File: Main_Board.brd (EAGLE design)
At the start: 160.3 x 95.4 mm, 222 parts, among them J1 SERVO, J2 5.5x2.1mm Barrel, J4 BATTERY, J5 SPEAKER, J6 SDIO-SDCARD, P1 MOTOR_HEADER, P2 MOTOR_HEADER, P3 JTAG, Q1 SI9933CDY-PFET, Q2 CSD17308Q3, Q3 CSD17308Q3, Q4 CSD17308Q3, Q5 CSD17308Q3, Q6 CSD17308Q3, Q7 CSD17308Q3, Q8 CSD17308Q3, U1 LMS8117, U10 IMU, U11 LTC3122-MSOP, U12 CBAT54S-SOT23-3, U13 BQ2947, U14 TPA2005D1DGN, U15 BQ40Z60, U2 5V_BUCK_REG, U3 BTM7752G, U4 BTM7752G, U5 SN74LV4T125, U6 SN74LV4T125, U7 STM32F405RGT6, U8 RN4020RN4020, U9 BQ51013B-20VQFN, Y1 32.768KHz, Y2 25MHz

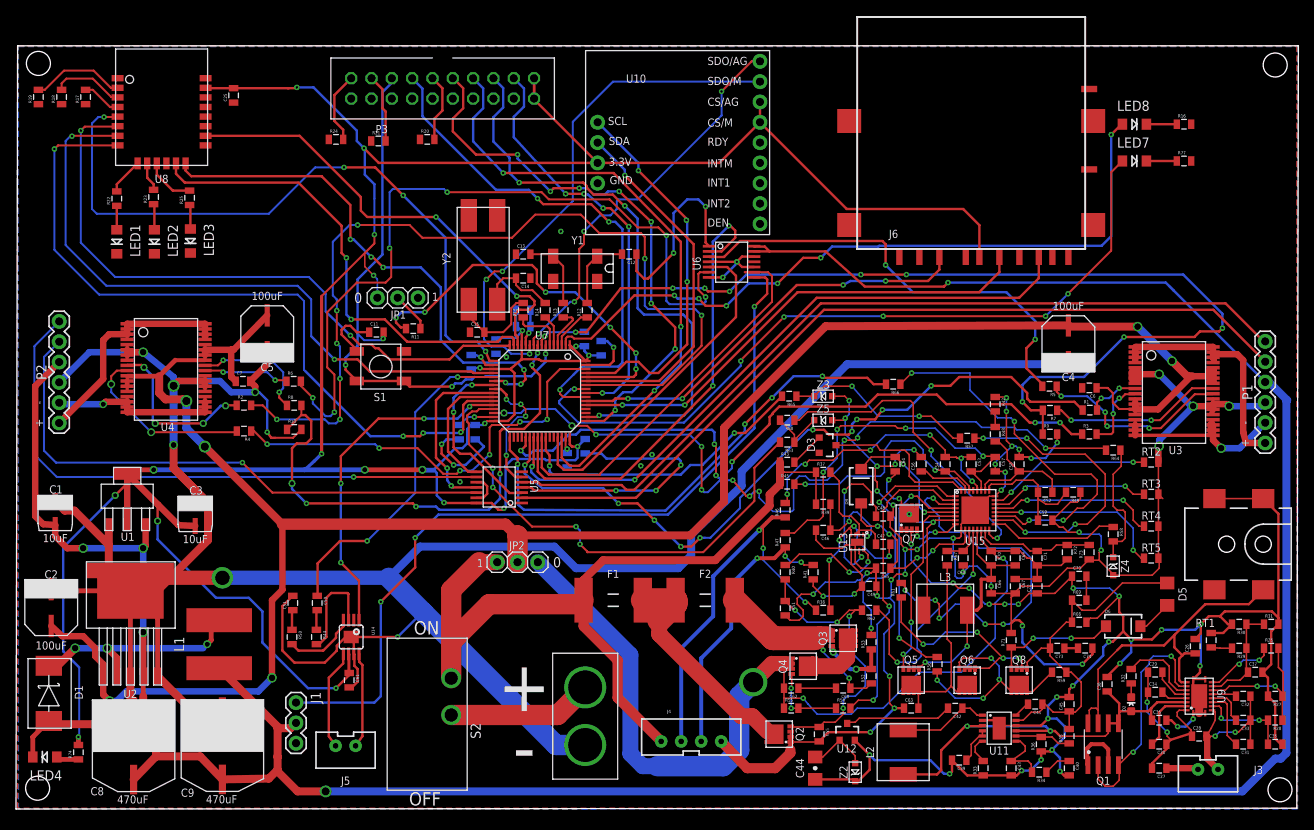
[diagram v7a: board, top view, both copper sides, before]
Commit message: added vias connecting top and bottom planes (also CAM output)
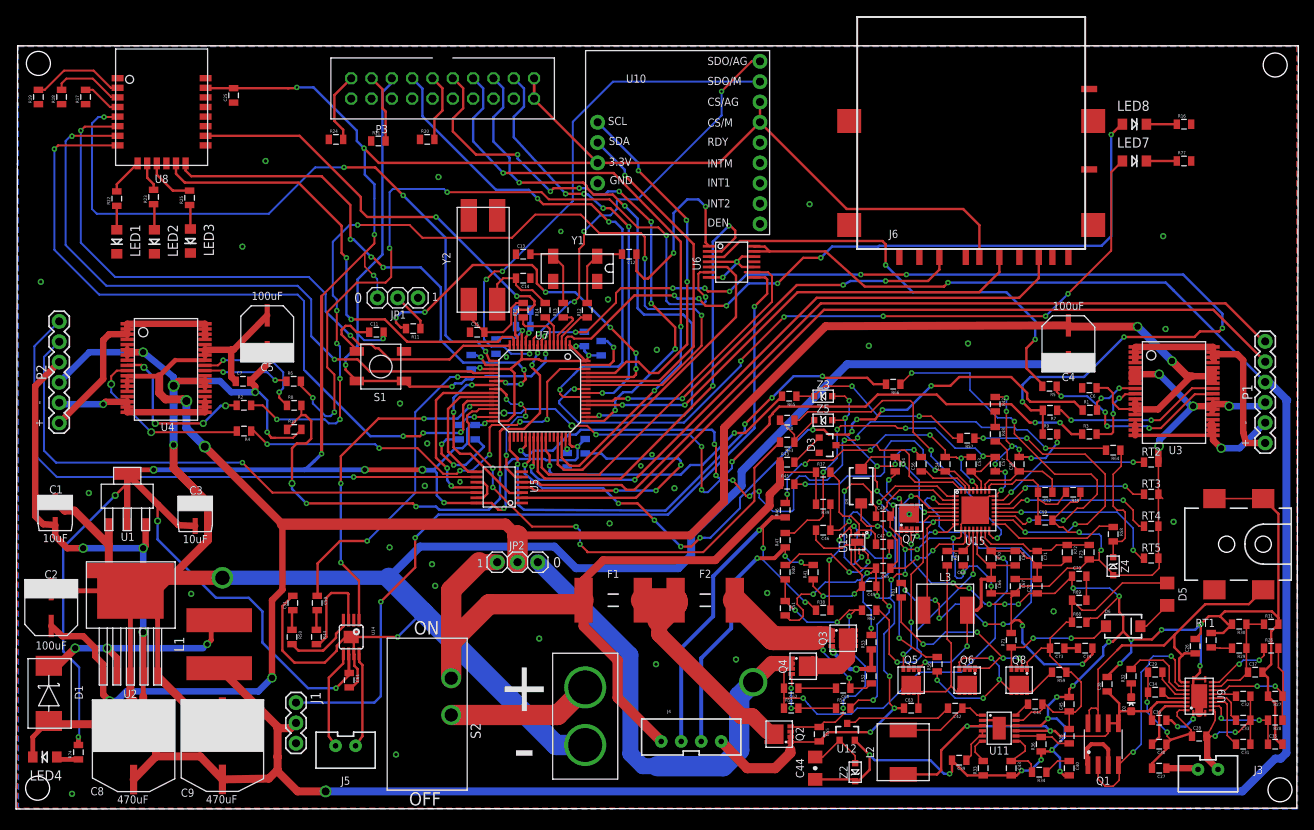
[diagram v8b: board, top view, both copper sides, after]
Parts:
- JP2: value SPDT_JUMPER -> IGNORE_CC
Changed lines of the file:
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@@
 <element name="FRAME2" library="SparkFun-Aesthetics" package="CREATIVE_COMMONS" value="FRAME-LEDGER" x="0" y="-20"/>
 <element name="FRAME3" library="SparkFun-Aesthetics" package="CREATIVE_COMMONS" value="FRAME-LEDGER" x="0" y="-20"/>
-<element name="JP2" library="BB8" package="1X03" value="SPDT_JUMPER" x="60.15" y="30.85"/>
+<element name="JP2" library="BB8" package="1X03" value="IGNORE_CC" x="60.15" y="30.85"/>
 <element name="FRAME4" library="SparkFun-Aesthetics" package="CREATIVE_COMMONS" value="FRAME-LEDGER" x="0" y="-20"/>
 <element name="FRAME5" library="SparkFun-Aesthetics" package="CREATIVE_COMMONS" value="FRAME-LEDGER" x="0" y="-20"/>
@@
 <wire x1="71.3" y1="59.6" x2="69.95" y2="59.6" width="0.3" layer="1"/>
 <via x="69.95" y="59.6" extent="1-16" drill="0.3"/>
-<wire x1="75.6" y1="65.1" x2="71.3" y2="59.6" width="0.3" layer="1"/>
 <wire x1="65.72" y1="58" x2="65.7" y2="58.02" width="0.254" layer="1"/>
 <wire x1="65.7" y1="58.02" x2="65.7" y2="58.6" width="0.254" layer="1"/>
@@
 <wire x1="66.1" y1="59.1" x2="66.6" y2="59.6" width="0.254" layer="16"/>
 <wire x1="66.6" y1="59.6" x2="69.95" y2="59.6" width="0.254" layer="16"/>
+<wire x1="71.3" y1="59.6" x2="75" y2="63.3" width="0.254" layer="1"/>
+<wire x1="75" y1="63.3" x2="75" y2="64.5" width="0.254" layer="1"/>
+<wire x1="75.6" y1="65.1" x2="75" y2="64.5" width="0.254" layer="1"/>
 </signal>
 <signal name="N$5">
@@
 <wire x1="92.9" y1="39.7" x2="92.9" y2="38.9" width="0.2" layer="16"/>
 <wire x1="59.72" y1="49.5" x2="61" y2="49.5" width="0.254" layer="1"/>
-<via x="61" y="49.5" extent="1-16" drill="0.5" shape="octagon"/>
+<via x="61" y="49.5" extent="1-16" drill="0.5"/>
 <wire x1="61" y1="49.5" x2="63.1" y2="49.5" width="0.254" layer="16"/>
 <wire x1="63.1" y1="49.5" x2="63.6" y2="50" width="0.254" layer="16"/>
@@
 <via x="68.1" y="72.2" extent="1-16" drill="0.3"/>
 </signal>
+<signal name="N$27">
+<via x="3.1" y="65.9" extent="1-16" drill="0.4"/>
+</signal>
+<signal name="N$43">
+<via x="28.3" y="70.3" extent="1-16" drill="0.4"/>
+</signal>
+<signal name="N$44">
+<via x="31.2" y="81" extent="1-16" drill="0.4"/>
+</signal>
+<signal name="N$45">
+<via x="99.2" y="75.6" extent="1-16" drill="0.4"/>
+</signal>
+<signal name="N$47">
+<via x="143.4" y="71.6" extent="1-16" drill="0.4"/>
+</signal>
+<signal name="N$130">
+<via x="106.6" y="57.9" extent="1-16" drill="0.4"/>
+</signal>
+<signal name="N$131">
+<via x="82.3" y="40.1" extent="1-16" drill="0.4"/>
+</signal>
+<signal name="N$132">
+<via x="74.2" y="35.7" extent="1-16" drill="0.4"/>
+</signal>
+<signal name="N$135">
+<via x="51.4" y="45.7" extent="1-16" drill="0.4"/>
+</signal>
+<signal name="N$136">
+<via x="51.1" y="40.4" extent="1-16" drill="0.4"/>
+</signal>
+<signal name="N$137">
+<via x="46.7" y="32.7" extent="1-16" drill="0.4"/>
+</signal>
+<signal name="N$138">
+<via x="52" y="30.6" extent="1-16" drill="0.4"/>
+</signal>
+<signal name="N$139">
+<via x="65.4" y="21.3" extent="1-16" drill="0.4"/>
+</signal>
+<signal name="N$140">
+<via x="90" y="18.7" extent="1-16" drill="0.4"/>
+</signal>
+<signal name="N$141">
+<via x="93.9" y="27" extent="1-16" drill="0.4"/>
+</signal>
+<signal name="N$142">
+<via x="129.7" y="24.7" extent="1-16" drill="0.4"/>
+</signal>
+<signal name="N$143">
+<via x="144.7" y="35.9" extent="1-16" drill="0.4"/>
+</signal>
+<signal name="N$144">
+<via x="143.7" y="60" extent="1-16" drill="0.4"/>
+</signal>
+<signal name="N$145">
+<via x="119" y="58.2" extent="1-16" drill="0.4"/>
+</signal>
+<signal name="N$146">
+<via x="52.4" y="27.9" extent="1-16" drill="0.4"/>
+</signal>
+<signal name="N$147">
+<via x="47.5" y="6.8" extent="1-16" drill="0.4"/>
+</signal>
+<signal name="N$148">
+<via x="7" y="1.9" extent="1-16" drill="0.4"/>
+</signal>
+<signal name="N$149">
+<via x="9.1" y="39.5" extent="1-16" drill="0.4"/>
+</signal>
+<signal name="N$150">
+<via x="21.9" y="26.9" extent="1-16" drill="0.4"/>
+</signal>
+<signal name="N$151">
+<via x="48" y="50.7" extent="1-16" drill="0.4"/>
+</signal>
+<signal name="N$152">
+<via x="80.1" y="57.4" extent="1-16" drill="0.4"/>
+</signal>
+<signal name="N$153">
+<via x="52.8" y="79" extent="1-16" drill="0.4"/>
+</signal>
+<signal name="N$154">
+<via x="80" y="18.1" extent="1-16" drill="0.4"/>
+</signal>
+<signal name="N$155">
+<via x="74" y="63.7" extent="1-16" drill="0.4"/>
+</signal>
 </signals>
